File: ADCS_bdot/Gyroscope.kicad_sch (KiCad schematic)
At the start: 1 part, among them U1 I3G4250DTR

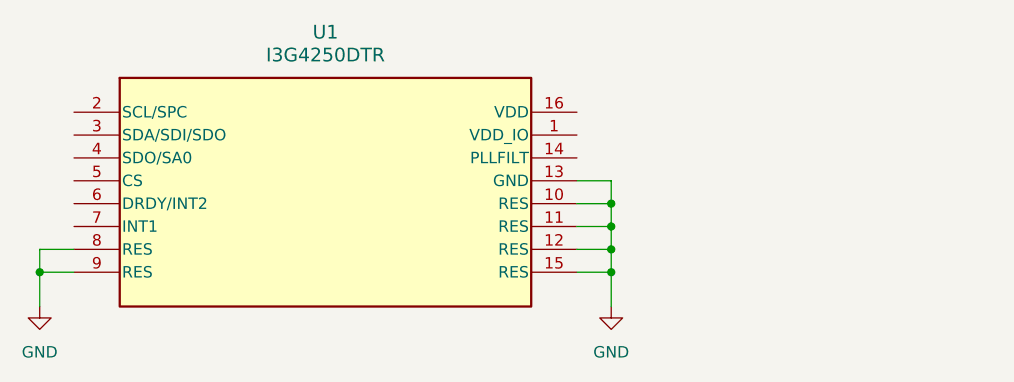
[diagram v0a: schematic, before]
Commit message: feat: Gyro and Mag RC Filter
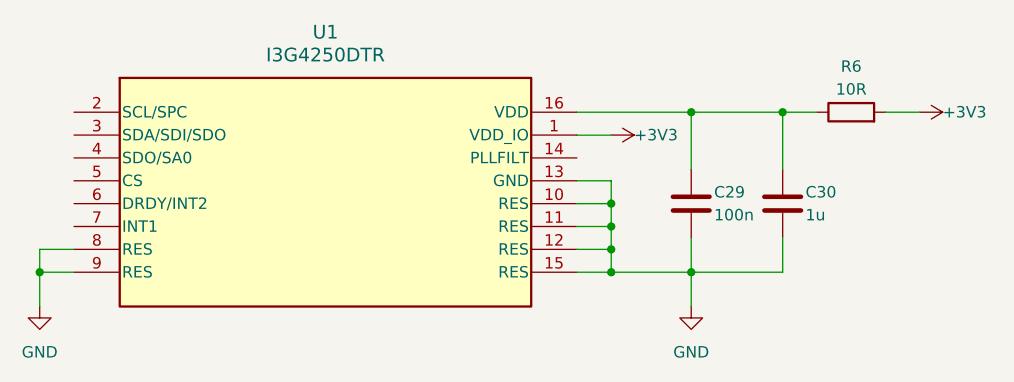
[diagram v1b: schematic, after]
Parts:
- added C29: 100n, symbol Device:C
- added C30: 1u, symbol Device:C
- added R6: 10R, symbol Device:R
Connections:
- net GND: now also C29.2, C30.2
- net +3V3: now reaches U1.1 (VDD_IO)
- net +3V3: now also R6.2
- net at U1.16 (VDD): now also C29.1, C30.1, R6.1
